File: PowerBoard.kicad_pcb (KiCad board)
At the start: 4 copper layers, 100 x 100 mm, 136 parts, among them Q2 PSMN020-100YS, Q3 PSMN020-100YS, Q4 PSMN020-100YS, U1 LT8342RV-TRMPBF, U10 LM5050-1, U11 PINA745AIRELR, U12 TPS16851VMAR, U13 LM5050-1, U14 TPS16851VMAR, U15 LM5050-1, U18 LMR43620MSC5RPERQ1, U2 AD5259BRMZ100, U3 ADAFRUIT_QT_PY, U9 TPS16851VMAR

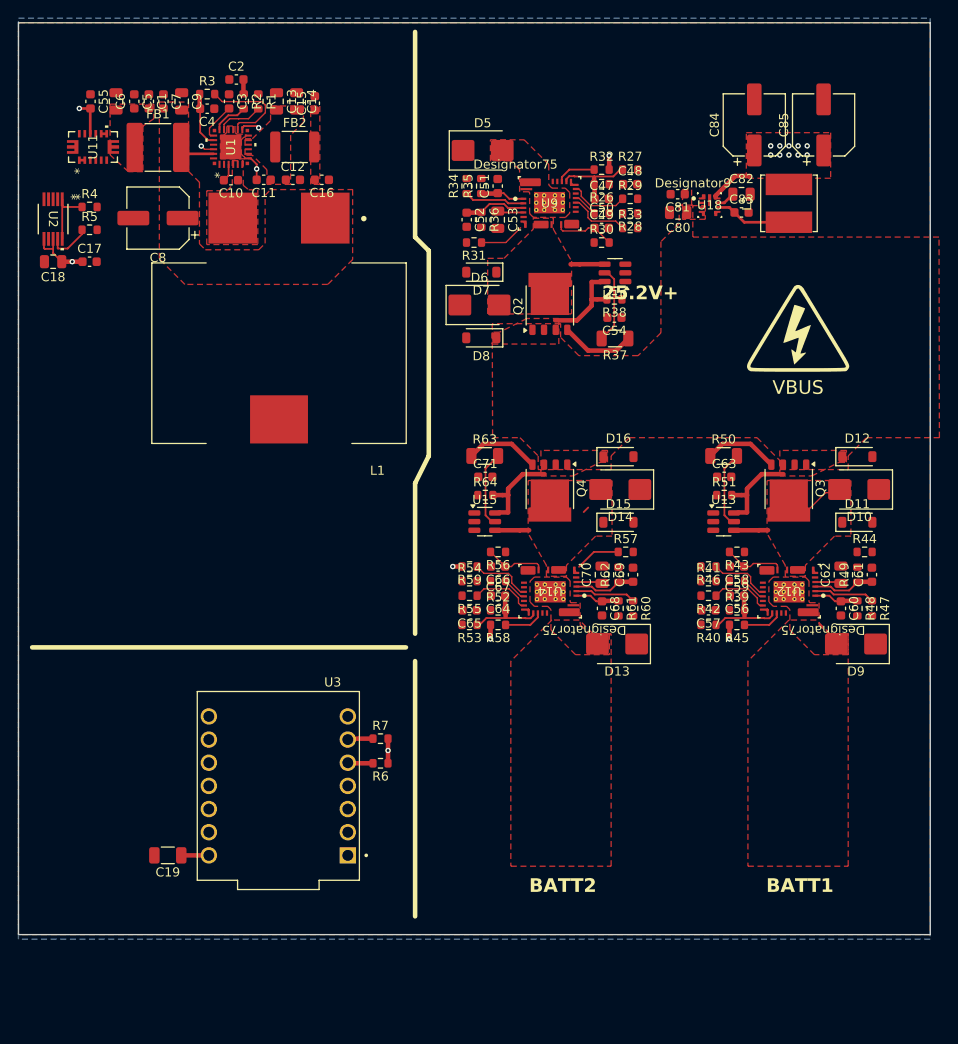
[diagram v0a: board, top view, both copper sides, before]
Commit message: Working on dev board for load switches
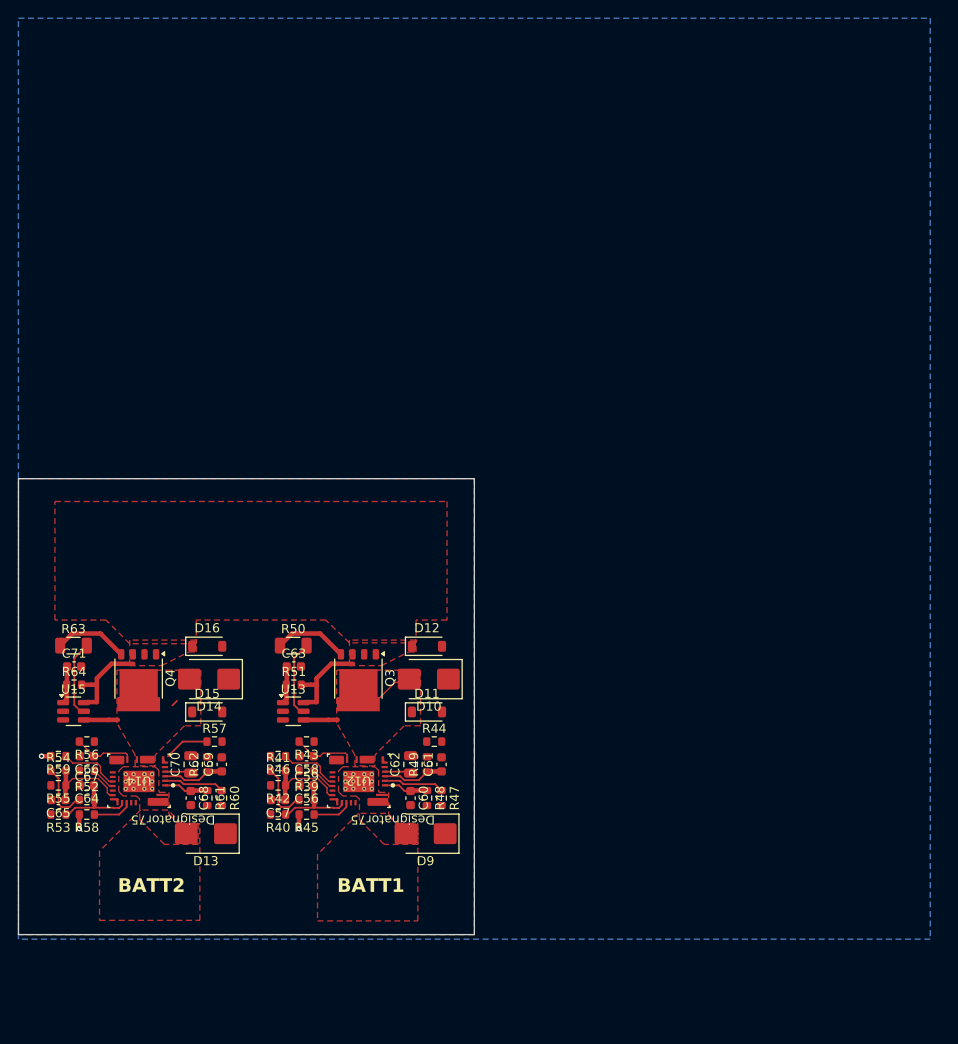
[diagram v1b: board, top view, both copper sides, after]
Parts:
- removed C1, C16: 220pF, Capacitor_SMD:C_0603_1608Metric
- removed C10, C11, C12, C15, C17, C3, C5, C54, C55, C7, C81, C83: 100nF, Capacitor_SMD:C_0603_1608Metric
- removed C13, C14, C18, C6, C9: 10uF, Capacitor_SMD:C_0805_2012Metric
- removed C19: 100nF, Capacitor_SMD:C_1206_3216Metric
- removed C2: 3.3nF, Capacitor_SMD:C_0603_1608Metric
- removed C4: 2.2uF, Capacitor_SMD:C_0603_1608Metric
- removed C47, C52: 100pF, Capacitor_SMD:C_0603_1608Metric
- removed C48: 10pF, Capacitor_SMD:C_0603_1608Metric
- removed C49: 0.22uF, Capacitor_SMD:C_0603_1608Metric
- removed C50: 4.7nF, Resistor_SMD:R_0603_1608Metric
- removed C51: 22pF, Capacitor_SMD:C_0603_1608Metric
- removed C53: 22nF, Capacitor_SMD:C_0805_2012Metric
- removed C8: 33uF, Capacitor_SMD:CP_Elec_6.3x5.8
- removed C80: 4.7uF, Capacitor_SMD:C_0805_2012Metric
- removed C82: 1uF, Capacitor_SMD:C_0805_2012Metric
- removed C84, C85: 22uF, Capacitor_SMD:CP_Elec_6.3x5.9
- removed D5, D6: TPSMB28CA-VR, Diode_SMD:D_SMB
- removed D7, D8: BAT46GWJ, Diode_SMD:D_SOD-123
- removed FB1: FerriteBead, Capacitor_SMD:C_2220_5750Metric
- removed FB2: 74279252, Inductor_SMD:L_1812_4532Metric
- removed G***: VBUS, LOGO
- removed L1: 33uH, _Power_Board:IND_SER2918H-333KL
- removed L3: 3.3uH, Inductor_SMD:L_Bourns_SRN6045TA
- removed NT4, NT5, NT6: NetTie_2, NetTie:NetTie-2_SMD_Pad0.5mm
- removed Q2: PSMN020-100YS, _Power_Board:LFPAK56_1
- removed R1: 31.6k, Resistor_SMD:R_0603_1608Metric
- removed R2: 60.4k, Resistor_SMD:R_0603_1608Metric
- removed R26, R28: 1Meg, Resistor_SMD:R_0603_1608Metric
- removed R27: 36k, Resistor_SMD:R_0603_1608Metric
- removed R29: 67.3k, Resistor_SMD:R_0603_1608Metric
- removed R3: 33.6k, Resistor_SMD:R_0603_1608Metric
- removed R30: 150, Resistor_SMD:R_0603_1608Metric
- removed R31: 240k, Resistor_SMD:R_0603_1608Metric
- removed R32, R33, R6, R7: 33k, Resistor_SMD:R_0603_1608Metric
- removed R34: 1.26k, Resistor_SMD:R_0603_1608Metric
- removed R35: 464, Resistor_SMD:R_0603_1608Metric
- removed R36: 1k, Resistor_SMD:R_0603_1608Metric
- removed R37: 10, Resistor_SMD:R_1206_3216Metric
- removed R38: 100, Resistor_SMD:R_0603_1608Metric
- removed R4: 15k, Resistor_SMD:R_0603_1608Metric
- removed R5: 274k, Resistor_SMD:R_0603_1608Metric
- removed U1: LT8342RV-TRMPBF, _Power_Board:05-08-7040_ADI
- removed U10: LM5050-1, Package_TO_SOT_SMD:TSOT-23-6
- removed U11: PINA745AIRELR, _Power_Board:REL0014A_PINA745AIRELR_TEX
- removed U18: LMR43620MSC5RPERQ1, _Power_Board:RPE0009A-MFG
- removed U2: AD5259BRMZ100, _Power_Board:RM_10_ADI
- removed U3: ADAFRUIT_QT_PY, _Power_Board:MODULE_ADAFRUIT_QT_PY
- removed U9: TPS16851VMAR, _Power_Board:VMA0023A-MFG
- moved C56 51.6 mm to (126.6, 128.1)
- moved C57 51.6 mm to (123.5, 129.7)
- moved C58 51.6 mm to (126.6, 124.9)
- moved C59 51.6 mm to (126.6, 126.5)
- moved NT9 51.6 mm to (126.6, 117.1)
- moved R39 51.6 mm to (126.6, 129.7)
- moved R40 51.6 mm to (123.5, 131.3)
- moved R41 51.6 mm to (123.5, 126.5)
- moved R42 51.6 mm to (123.5, 128.1)
- moved R43 51.6 mm to (126.6, 123.3)
- moved R44 51.6 mm to (140.6, 123.3)
- moved R45 51.6 mm to (126.6, 131.3)
- moved R46 51.6 mm to (123.5, 124.9)
- moved C63 51.6 mm to (125.2, 115.1)
- moved NT8 51.6 mm to (127.2, 119.0)
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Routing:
- net +5V: track 27.4 -> 4.10 mm, vias 17 -> 3
- net Net-(U1-VSET1): track 11.0 -> 0.00 mm
- net Net-(U9-OVP): track 9.21 -> 0.00 mm
- net Net-(U18-BOOT): track 8.47 -> 0.00 mm
- net Net-(U10-GATE): track 8.41 -> 0.00 mm
- net Net-(Q2-PadG): track 8.19 -> 0.00 mm
- net VBUS: track 23.6 -> 15.7 mm
- net Net-(U2-A): track 7.27 -> 0.00 mm
- net Net-(U9-IREF): track 6.78 -> 0.00 mm
- net /Main/batt1_load_sw/IN: track 0.00 -> 6.75 mm
- net /Main/batt2_load_sw/IN: track 0.00 -> 6.75 mm
- net /Main/BOOSTX.FLTn: track 6.70 -> 0.00 mm
- net Net-(U9-VDD): track 6.67 -> 0.00 mm
- net /Main/BOOSTX.IMON: track 6.65 -> 0.00 mm
- net Net-(U9-EN_UVLO): track 6.52 -> 0.00 mm
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- removed copper zone on F.Cu, net +5V
- removed copper zone on F.Cu, net /Main/boost_a_frontend/BOOST_OUT
- removed copper zone on F.Cu, net /Main/boost_a_frontend/PANEL_IN
- removed copper zone on F.Cu, net /Main/boost_a_frontend/Vout
- removed copper zone on F.Cu, net Net-(C10-Pad1)
- removed copper zone on F.Cu, net Net-(D6-A2)
- removed copper zone on F.Cu, net Net-(U1-VIN)
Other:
- board size 100 x 100 mm -> 50 x 50 mm
- board text removed: "25.2V+"

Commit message: Working on tp
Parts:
- added H1: MountingHole_Pad_MP, TestPoint:TestPoint_Pad_4.0x4.0mm, F.Cu at (132.5, 151.0)
- added H2: MountingHole_Pad_MP, TestPoint:TestPoint_Pad_4.0x4.0mm, F.Cu at (123.5, 151.0)
- added H3: MountingHole_Pad_MP, TestPoint:TestPoint_Pad_4.0x4.0mm, F.Cu at (108.5, 151.0)
- added H4: MountingHole_Pad_MP, TestPoint:TestPoint_Pad_4.0x4.0mm, F.Cu at (117.5, 151.0)
- added H5: MountingHole_Pad_MP, TestPoint:TestPoint_Pad_4.0x4.0mm, F.Cu at (141.5, 100.5)
- added H6: MountingHole_Pad_MP, TestPoint:TestPoint_Pad_4.0x4.0mm, F.Cu at (141.5, 106.5)
- added TP11: BATT2_DRV_RTN, TestPoint:TestPoint_Plated_Hole_D5.0mm, F.Cu at (121.0, 103.5)
- added TP12: BATT2_DRV_RTN, TestPoint:TestPoint_Plated_Hole_D5.0mm, F.Cu at (109.0, 103.5)
- added TP7: BATT1_DRV_TP, TestPoint:TestPoint_Plated_Hole_D5.0mm, F.Cu at (132.5, 142.0)
- added TP8: BATT1_RTN_TP, TestPoint:TestPoint_Plated_Hole_D5.0mm, F.Cu at (120.5, 142.0)
- added TP9: BATT2_DRV_RTN, TestPoint:TestPoint_Plated_Hole_D5.0mm, F.Cu at (108.5, 142.0)
- moved C60 0.76 mm to (137.2, 129.5)
- moved C61 0.76 mm to (140.6, 125.8)
- moved C62 0.76 mm to (137.2, 125.8)
- moved C63 0.76 mm to (124.4, 115.1)
- moved C64 0.76 mm to (101.7, 128.1)
- moved C65 0.76 mm to (98.6, 129.7)
- moved C66 0.76 mm to (101.7, 124.9)
- moved C67 0.76 mm to (101.7, 126.5)
- moved C68 0.76 mm to (113.1, 129.5)
- moved C70 0.76 mm to (113.1, 125.8)
- moved D10 0.76 mm to (139.2, 116.5)
- moved D11 0.76 mm to (139.0, 120.1)
- moved D12 0.76 mm to (139.0, 112.9)
- moved D14 0.76 mm to (115.1, 116.5)
- moved D15 0.76 mm to (114.9, 120.1)
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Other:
- board size 50 x 50 mm -> 50 x 60 mm
- board text added: "VBUS"

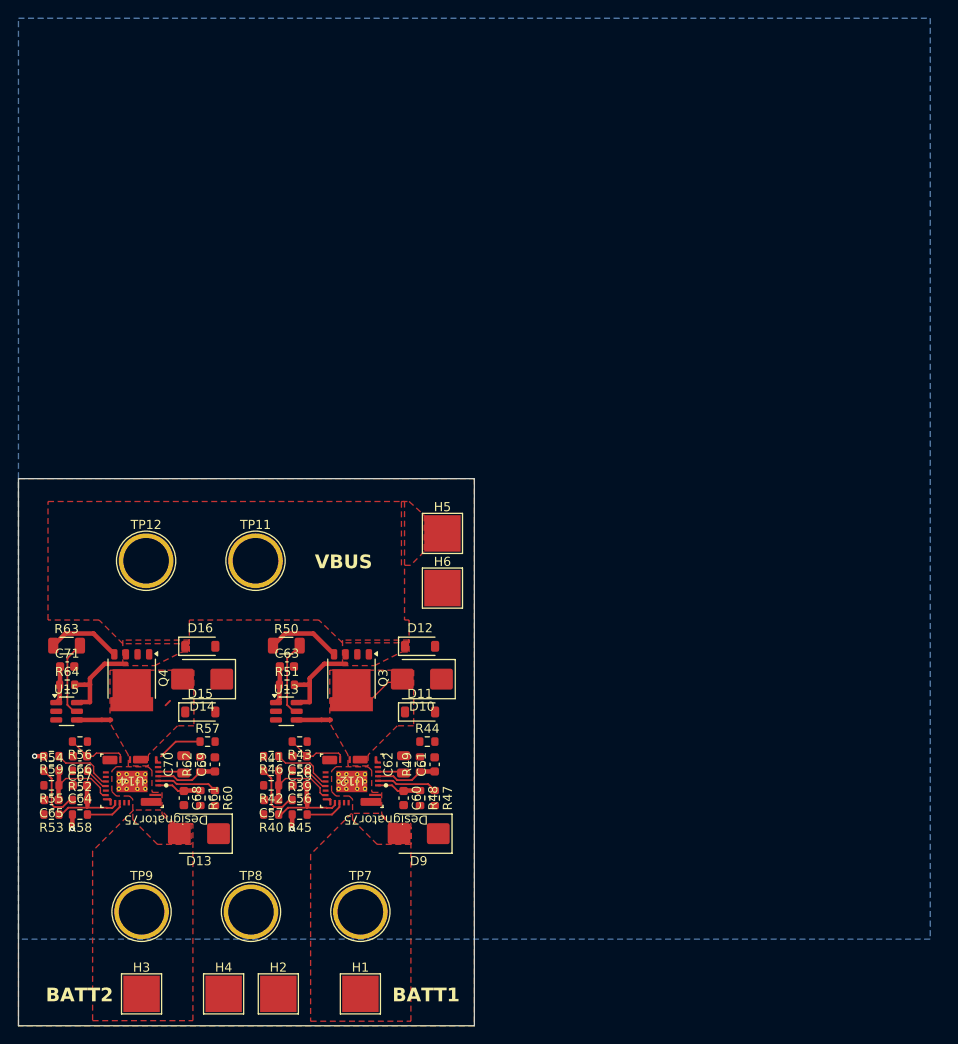
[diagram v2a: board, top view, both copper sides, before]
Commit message: Adding LED drivers and enable switch
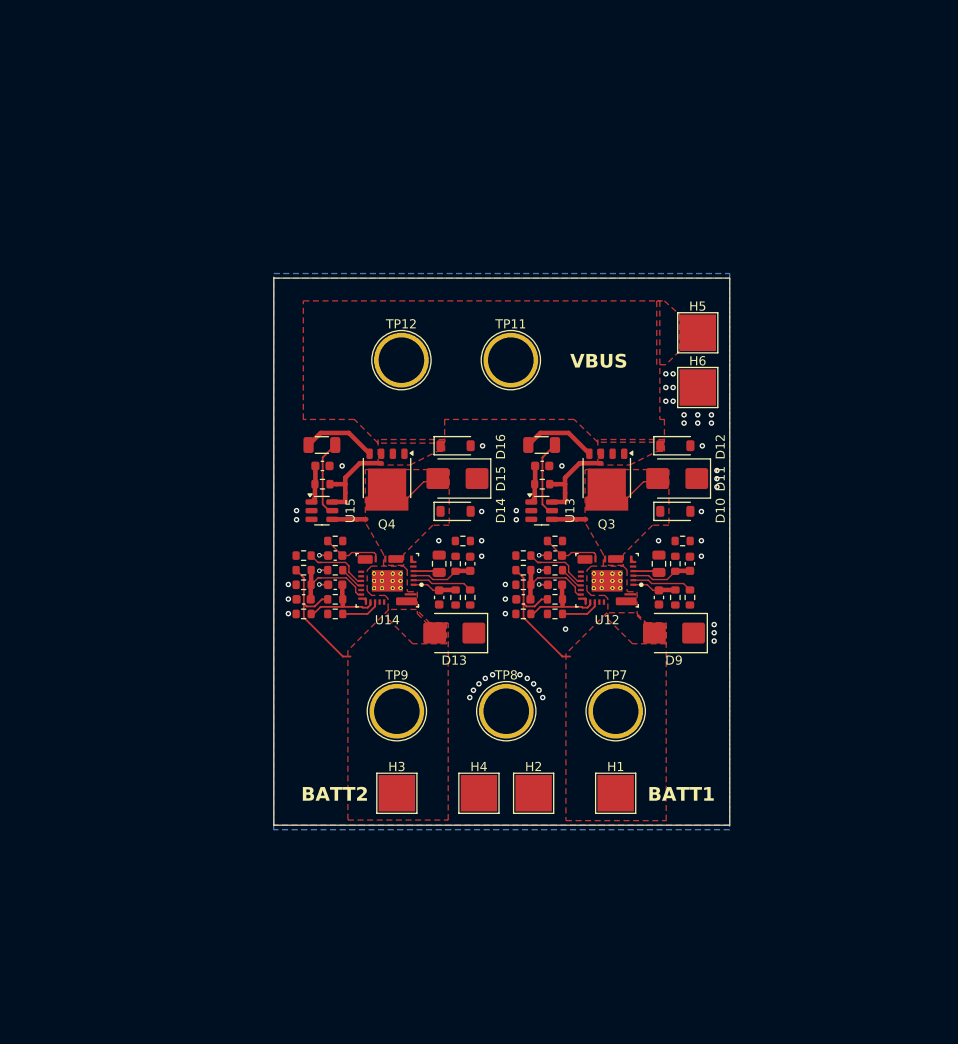
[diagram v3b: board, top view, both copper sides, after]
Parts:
- moved NT11 36.3 mm to (130.8, 96.5), turned to 90 degrees
- moved NT8 36.3 mm to (154.9, 96.5), turned to 90 degrees
- moved NT12 36.1 mm to (130.3, 95.1)
- moved NT9 36.1 mm to (154.4, 95.1)
- moved C63 35.6 mm to (152.4, 93.1)
- moved D15 35.6 mm to (142.9, 98.1)
- moved D16 35.6 mm to (142.9, 90.9)
- moved R50 35.6 mm to (152.4, 90.8)
- moved R51 35.6 mm to (152.4, 95.1)
- moved R61 35.6 mm to (142.9, 107.5)
- moved R62 35.6 mm to (142.9, 103.8)
- moved U13 35.6 mm to (152.4, 98.0)
- moved C64 35.6 mm to (129.7, 106.1)
- moved C56 35.6 mm to (153.8, 106.1)
- moved C60 35.6 mm to (165.2, 107.5)
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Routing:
- net /Main/batt2_load_sw/IN: track 6.75 -> 15.8 mm
- net /Main/batt1_load_sw/IN: track 6.75 -> 15.8 mm
- net Net-(D14-A2): track 0.00 -> 5.67 mm
- net GND: track 0.70 -> 5.81 mm, vias 0 -> 57
- net Net-(U14-SFT_SEL): track 4.96 -> 0.00 mm
- net +5V: track 4.10 -> 0.00 mm, vias 3 -> 0
- net VBUS: track 15.7 -> 12.6 mm
- net Net-(U15-OUT): track 0.00 -> 1.44 mm
- net Net-(U13-OUT): track 0.00 -> 1.44 mm
- net Net-(NT9-Pad1): track 0.00 -> 0.68 mm
- net Net-(NT12-Pad1): track 0.00 -> 0.68 mm
- removed copper zone on In2.Cu, net +5V
- removed copper zone on In1.Cu, net GND
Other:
- copper layers 4 -> 2
